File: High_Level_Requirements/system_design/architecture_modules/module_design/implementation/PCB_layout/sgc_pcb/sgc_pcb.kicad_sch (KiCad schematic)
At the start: 44 parts, among them J1 BAT_JST, Q1 PMOS_RFID, Q2 PMOS_UWB, SW1 Langir_16mm_Piezo, U1 LDC1612DNTR, U10 74AHCT1G125, U11 IP6833, U4 MT3608, U5 BHI260AP, U6 BMP390, U7 MX25R1635F, U8 IS31FL3194, U9 BQ25120A

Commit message: hw(v4.2): MX25R6435F 8MB flash + USB-C charging (drop Qi, beeper DNP)
- Flash U7: MX25R1635F (2MB) -> MX25R6435F (8MB), pin-compatible SOIC-8
  208-mil + JEDEC SPI/SFDP. Firmware auto-detects size (other session).
- Qi receiver (IP6833 + coil + passives) -> DNP; replaced by USB-C charging
  (GCT USB4085-GF-A, CC 5.1k sink pull-downs, ESD TVS, IP67 tethered cap).
- Beeper BZ1 -> DNP (footprint retained).
- Battery JST 3-pin flagged provisional.
- Discrepancy fixes: Y1 crystal + U6 BMP390 added to ref, stale "Reed
  Switch" label -> Langir piezo, rev v1.0 -> v4.2.
- New doc: sgc_usb_c_charging_spec.md.
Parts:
- removed U7: MX25R1635F, Package_SO:SOIC-8_3.9x4.9mm_P1.27mm, symbol sgc_pcb_symbols:MX25R1635F
- added C_USB: 10uF, Capacitor_SMD:C_0805_2012Metric, symbol Device:C
- added J2: USB4085, Connector_USB:USB_C_Receptacle_USB2.0, symbol Connector:USB_C_Receptacle_USB2.0
- added R_CC1, R_CC2: 5.1k, Resistor_SMD:R_0402_1005Metric, symbol Device:R
- added U7: MX25R6435F, Package_SO:SOIC-8_5.23x5.23mm_P1.27mm, symbol sgc_pcb_symbols:MX25R6435F
- added Y1: 32.768kHz, Crystal:Crystal_SMD_3215-2Pin_3.2x1.5mm, symbol Device:Crystal
- BZ1, C_AC1, C_AC2, C_BOOT, C_RECT, C_VDD, L3, U11: now not fitted; now left out of the parts list
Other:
- note added: "Sheet 2 — Sensors: Langir Piezo Button (v1 arming) + LDC1612 (v2, DNP)"
- note added: "Sheet 3 — Peripherals: SK6812 ×5 + Level Shifter + Beeper (DNP)"
- note added: "Sheet 4 — Power: Boost MT3608 + Battery JST + USB-C Charging (Qi DNP)"
- note removed: "Sheet 2 — Sensors: Reed Switch (v1 arming) + LDC1612 (v2, DNP)"
- note removed: "Sheet 3 — Peripherals: SK6812 ×5 + Level Shifter + Beeper"
- note removed: "Sheet 4 — Power: Boost MT3608 + Qi IP6833 + Battery JST"
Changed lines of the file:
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@@
   (title_block
     (title "SGC — Ski Gate Chrono")
-    (date "2026-08-12")
-    (rev "v1.0")
+    (date "2026-08-13")
+    (rev "v4.2")
     (company "VYT Solutions")
     (comment 1 "Custom PCB — Nicla Sense ME Replica")
-    (comment 2 "22 × 55 mm, 4-layer FR4, 0.8 mm")
+    (comment 2 "22 × 55 mm, 4-layer FR4, 0.8 mm — 8 MB flash + USB-C charging")
   )
   (symbol (lib_id "sgc_pcb_symbols:ANNA-B112") (at 200 300 0) (unit 1)
@@
     (instances (project "sgc_pcb" (path "/a1b2c3d4-e5f6-4a7b-8c9d-0e1f2a3b4c5d" (reference "MD1") (unit 1))))
   )
+  (symbol (lib_id "Device:Crystal") (at 150 200 0) (unit 1)
+    (exclude_from_sim no) (in_bom yes) (on_board yes) (dnp no)
+    (property "Reference" "Y1" (at 150 160 0) (effects (font (size 1.27 1.27))))
+    (property "Value" "32.768kHz" (at 150 240 0) (effects (font (size 1.27 1.27))))
+    (property "Footprint" "Crystal:Crystal_SMD_3215-2Pin_3.2x1.5mm" (at 150 200 0) (effects (font (size 1.27 1.27)) hide))
+    (instances (project "sgc_pcb" (path "/a1b2c3d4-e5f6-4a7b-8c9d-0e1f2a3b4c5d" (reference "Y1") (unit 1))))
+  )
   (symbol (lib_id "sgc_pcb_symbols:BHI260AP") (at 600 300 0) (unit 1)
     (exclude_from_sim no) (in_bom yes) (on_board yes) (dnp no)
@@
     (instances (project "sgc_pcb" (path "/a1b2c3d4-e5f6-4a7b-8c9d-0e1f2a3b4c5d" (reference "U6") (unit 1))))
   )
-  (symbol (lib_id "sgc_pcb_symbols:MX25R1635F") (at 600 100 0) (unit 1)
+  (symbol (lib_id "sgc_pcb_symbols:MX25R6435F") (at 600 100 0) (unit 1)
     (exclude_from_sim no) (in_bom yes) (on_board yes) (dnp no)
     (property "Reference" "U7" (at 600 60 0) (effects (font (size 1.27 1.27))))
-    (property "Value" "MX25R1635F" (at 600 140 0) (effects (font (size 1.27 1.27))))
-    (property "Footprint" "Package_SO:SOIC-8_3.9x4.9mm_P1.27mm" (at 600 100 0) (effects (font (size 1.27 1.27)) hide))
+    (property "Value" "MX25R6435F" (at 600 140 0) (effects (font (size 1.27 1.27))))
+    (property "Footprint" "Package_SO:SOIC-8_5.23x5.23mm_P1.27mm" (at 600 100 0) (effects (font (size 1.27 1.27)) hide))
     (instances (project "sgc_pcb" (path "/a1b2c3d4-e5f6-4a7b-8c9d-0e1f2a3b4c5d" (reference "U7") (unit 1))))
   )
@@
   )
   (symbol (lib_id "sgc_pcb_symbols:Piezo_Transducer") (at 300 650 0) (unit 1)
-    (exclude_from_sim no) (in_bom yes) (on_board yes) (dnp no)
+    (exclude_from_sim no) (in_bom no) (on_board no) (dnp yes)
     (property "Reference" "BZ1" (at 300 610 0) (effects (font (size 1.27 1.27))))
     (property "Value" "Piezo_10x10" (at 300 690 0) (effects (font (size 1.27 1.27))))
@@
   )
   (symbol (lib_id "sgc_pcb_symbols:IP6833") (at 800 -300 0) (unit 1)
-    (exclude_from_sim no) (in_bom yes) (on_board yes) (dnp no)
+    (exclude_from_sim no) (in_bom no) (on_board no) (dnp yes)
     (property "Reference" "U11" (at 800 -340 0) (effects (font (size 1.27 1.27))))
     (property "Value" "IP6833" (at 800 -260 0) (effects (font (size 1.27 1.27))))
@@
   )
   (symbol (lib_id "sgc_pcb_symbols:Qi_Coil") (at 800 -500 0) (unit 1)
-    (exclude_from_sim no) (in_bom yes) (on_board yes) (dnp no)
+    (exclude_from_sim no) (in_bom no) (on_board no) (dnp yes)
     (property "Reference" "L3" (at 800 -540 0) (effects (font (size 1.27 1.27))))
     (property "Value" "24uH_A11" (at 800 -460 0) (effects (font (size 1.27 1.27))))
@@
     (instances (project "sgc_pcb" (path "/a1b2c3d4-e5f6-4a7b-8c9d-0e1f2a3b4c5d" (reference "J1") (unit 1))))
   )
+  (symbol (lib_id "Connector:USB_C_Receptacle_USB2.0") (at 800 -600 0) (unit 1)
+    (exclude_from_sim no) (in_bom yes) (on_board yes) (dnp no)
+    (property "Reference" "J2" (at 800 -640 0) (effects (font (size 1.27 1.27))))
+    (property "Value" "USB4085" (at 800 -560 0) (effects (font (size 1.27 1.27))))
+    (property "Footprint" "Connector_USB:USB_C_Receptacle_USB2.0" (at 800 -600 0) (effects (font (size 1.27 1.27)) hide))
+    (instances (project "sgc_pcb" (path "/a1b2c3d4-e5f6-4a7b-8c9d-0e1f2a3b4c5d" (reference "J2") (unit 1))))
+  )
   (symbol (lib_id "sgc_pcb_symbols:PMOS_Gate") (at 900 500 0) (unit 1)
     (exclude_from_sim no) (in_bom no) (on_board no) (dnp yes)
@@
   )
   (symbol (lib_id "Device:C") (at 850 -400 0) (unit 1)
-    (exclude_from_sim no) (in_bom yes) (on_board yes) (dnp no)
+    (exclude_from_sim no) (in_bom no) (on_board no) (dnp yes)
     (property "Reference" "C_AC1" (at 850 -440 0) (effects (font (size 1.27 1.27))))
     (property "Value" "22nF" (at 850 -360 0) (effects (font (size 1.27 1.27))))
@@
   )
   (symbol (lib_id "Device:C") (at 850 -450 0) (unit 1)
-    (exclude_from_sim no) (in_bom yes) (on_board yes) (dnp no)
+    (exclude_from_sim no) (in_bom no) (on_board no) (dnp yes)
     (property "Reference" "C_AC2" (at 850 -490 0) (effects (font (size 1.27 1.27))))
     (property "Value" "22nF" (at 850 -410 0) (effects (font (size 1.27 1.27))))
@@
   )
   (symbol (lib_id "Device:C") (at 900 -300 0) (unit 1)
-    (exclude_from_sim no) (in_bom yes) (on_board yes) (dnp no)
+    (exclude_from_sim no) (in_bom no) (on_board no) (dnp yes)
     (property "Reference" "C_RECT" (at 900 -340 0) (effects (font (size 1.27 1.27))))
     (property "Value" "22uF" (at 900 -260 0) (effects (font (size 1.27 1.27))))
@@
   )
   (symbol (lib_id "Device:C") (at 900 -350 0) (unit 1)
-    (exclude_from_sim no) (in_bom yes) (on_board yes) (dnp no)
+    (exclude_from_sim no) (in_bom no) (on_board no) (dnp yes)
     (property "Reference" "C_BOOT" (at 900 -390 0) (effects (font (size 1.27 1.27))))
     (property "Value" "100n" (at 900 -310 0) (effects (font (size 1.27 1.27))))
@@
   )
   (symbol (lib_id "Device:C") (at 900 -400 0) (unit 1)
-    (exclude_from_sim no) (in_bom yes) (on_board yes) (dnp no)
+    (exclude_from_sim no) (in_bom no) (on_board no) (dnp yes)
     (property "Reference" "C_VDD" (at 900 -440 0) (effects (font (size 1.27 1.27))))
     (property "Value" "1uF" (at 900 -360 0) (effects (font (size 1.27 1.27))))
@@
     (instances (project "sgc_pcb" (path "/a1b2c3d4-e5f6-4a7b-8c9d-0e1f2a3b4c5d" (reference "L_Boost") (unit 1))))
   )
+  (symbol (lib_id "Device:R") (at 900 -600 0) (unit 1)
+    (exclude_from_sim no) (in_bom yes) (on_board yes) (dnp no)
+    (property "Reference" "R_CC1" (at 900 -640 0) (effects (font (size 1.27 1.27))))
+    (property "Value" "5.1k" (at 900 -560 0) (effects (font (size 1.27 1.27))))
+    (property "Footprint" "Resistor_SMD:R_0402_1005Metric" (at 900 -600 0) (effects (font (size 1.27 1.27)) hide))
+    (instances (project "sgc_pcb" (path "/a1b2c3d4-e5f6-4a7b-8c9d-0e1f2a3b4c5d" (reference "R_CC1") (unit 1))))
+  )
+  (symbol (lib_id "Device:R") (at 900 -650 0) (unit 1)
+    (exclude_from_sim no) (in_bom yes) (on_board yes) (dnp no)
+    (property "Reference" "R_CC2" (at 900 -690 0) (effects (font (size 1.27 1.27))))
+    (property "Value" "5.1k" (at 900 -610 0) (effects (font (size 1.27 1.27))))
+    (property "Footprint" "Resistor_SMD:R_0402_1005Metric" (at 900 -650 0) (effects (font (size 1.27 1.27)) hide))
+    (instances (project "sgc_pcb" (path "/a1b2c3d4-e5f6-4a7b-8c9d-0e1f2a3b4c5d" (reference "R_CC2") (unit 1))))
+  )
+  (symbol (lib_id "Device:C") (at 900 -700 0) (unit 1)
+    (exclude_from_sim no) (in_bom yes) (on_board yes) (dnp no)
+    (property "Reference" "C_USB" (at 900 -740 0) (effects (font (size 1.27 1.27))))
+    (property "Value" "10uF" (at 900 -660 0) (effects (font (size 1.27 1.27))))
+    (property "Footprint" "Capacitor_SMD:C_0805_2012Metric" (at 900 -700 0) (effects (font (size 1.27 1.27)) hide))
+    (instances (project "sgc_pcb" (path "/a1b2c3d4-e5f6-4a7b-8c9d-0e1f2a3b4c5d" (reference "C_USB") (unit 1))))
+  )
   (symbol (lib_id "power:VCC_3V3") (at 700 -600 0) (unit 1)
     (exclude_from_sim no) (in_bom yes) (on_board yes) (dnp no)
@@
     (instances (project "sgc_pcb" (path "/a1b2c3d4-e5f6-4a7b-8c9d-0e1f2a3b4c5d" (reference "#PWR") (unit 1))))
   )
-  (symbol (lib_id "power:V_QI_5V") (at 1100 -600 0) (unit 1)
+  (symbol (lib_id "power:VBUS") (at 1100 -600 0) (unit 1)
     (exclude_from_sim no) (in_bom yes) (on_board yes) (dnp no)
     (property "Reference" "#PWR" (at 1100 -600 0) (effects (font (size 1.27 1.27)) hide))
-    (property "Value" "V_QI_5V" (at 1100 -570 0) (effects (font (size 1.27 1.27))))
+    (property "Value" "VBUS" (at 1100 -570 0) (effects (font (size 1.27 1.27))))
     (instances (project "sgc_pcb" (path "/a1b2c3d4-e5f6-4a7b-8c9d-0e1f2a3b4c5d" (reference "#PWR") (unit 1))))
   )
@@
     (property "Intersheetrefs" "${INTERSHEET_REFS}" (at 450 600 0) (effects (font (size 1.27 1.27)) hide))
   )
-  (global_label "V_QI_5V" (shape bidirectional) (at 550 600 0) (fields_autoplaced yes)
+  (global_label "VBUS" (shape bidirectional) (at 550 600 0) (fields_autoplaced yes)
     (effects (font (size 1.27 1.27)) (justify left))
     (property "Intersheetrefs" "${INTERSHEET_REFS}" (at 550 600 0) (effects (font (size 1.27 1.27)) hide))
@@
   (text "SGC — Custom PCB: Nicla Sense ME Replica (v1 pole-mount)" (at 200 1200 0) (effects (font (size 2.0 2.0) bold)))
   (text "Sheet 1 — MCU Core: ANNA-B112 + BHI260AP + BMP390 + Flash + RGB + Charger" (at 200 400 0) (effects (font (size 2.0 2.0) bold)))
-  (text "Sheet 2 — Sensors: Reed Switch (v1 arming) + LDC1612 (v2, DNP)" (at 100 -200 0) (effects (font (size 2.0 2.0) bold)))
-  (text "Sheet 3 — Peripherals: SK6812 ×5 + Level Shifter + Beeper" (at 100 750 0) (effects (font (size 2.0 2.0) bold)))
-  (text "Sheet 4 — Power: Boost MT3608 + Qi IP6833 + Battery JST" (at 600 -150 0) (effects (font (size 2.0 2.0) bold)))
+  (text "Sheet 2 — Sensors: Langir Piezo Button (v1 arming) + LDC1612 (v2, DNP)" (at 100 -200 0) (effects (font (size 2.0 2.0) bold)))
+  (text "Sheet 3 — Peripherals: SK6812 ×5 + Level Shifter + Beeper (DNP)" (at 100 750 0) (effects (font (size 2.0 2.0) bold)))
+  (text "Sheet 4 — Power: Boost MT3608 + Battery JST + USB-C Charging (Qi DNP)" (at 600 -150 0) (effects (font (size 2.0 2.0) bold)))
   (text "Sheet 5 — v2 Peripherals (UNPOPULATED): RFID + UWB power gates" (at 900 700 0) (effects (font (size 2.0 2.0) bold)))
 )

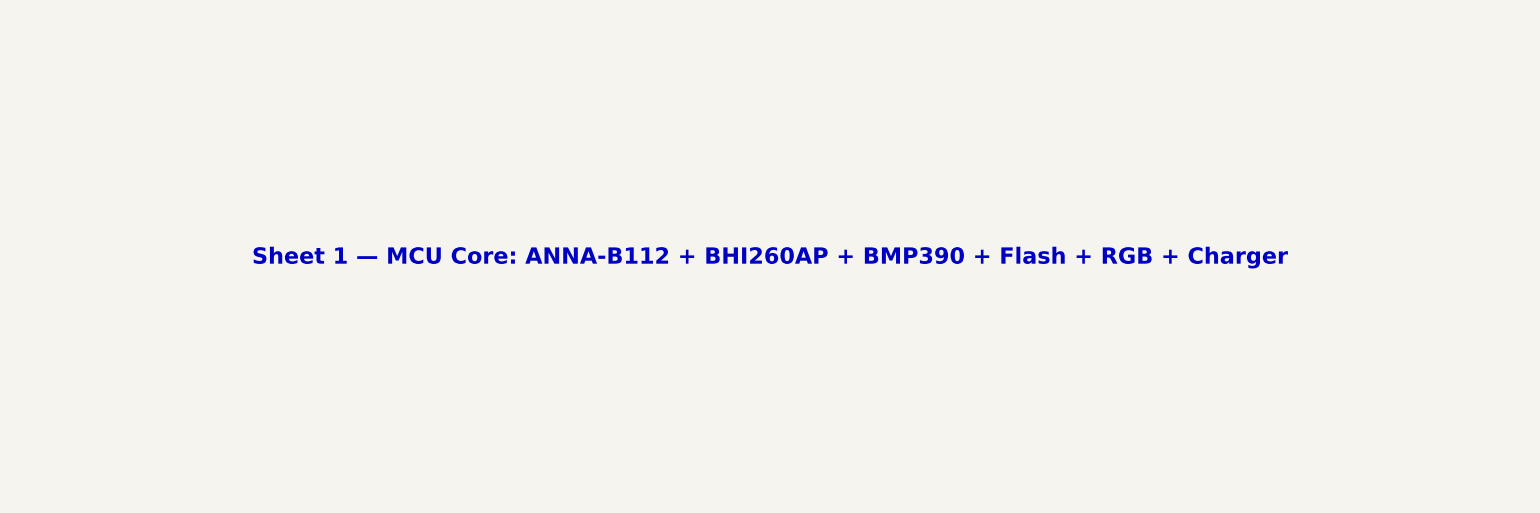
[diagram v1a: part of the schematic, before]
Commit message: hw: ANNA-B412 (nRF52833) as production MD1 — docs + schematic
Park production-module swap on branch until custom board exists.
Master stays Nicla/nRF52832 day-to-day. See anna_b412_migration.md.
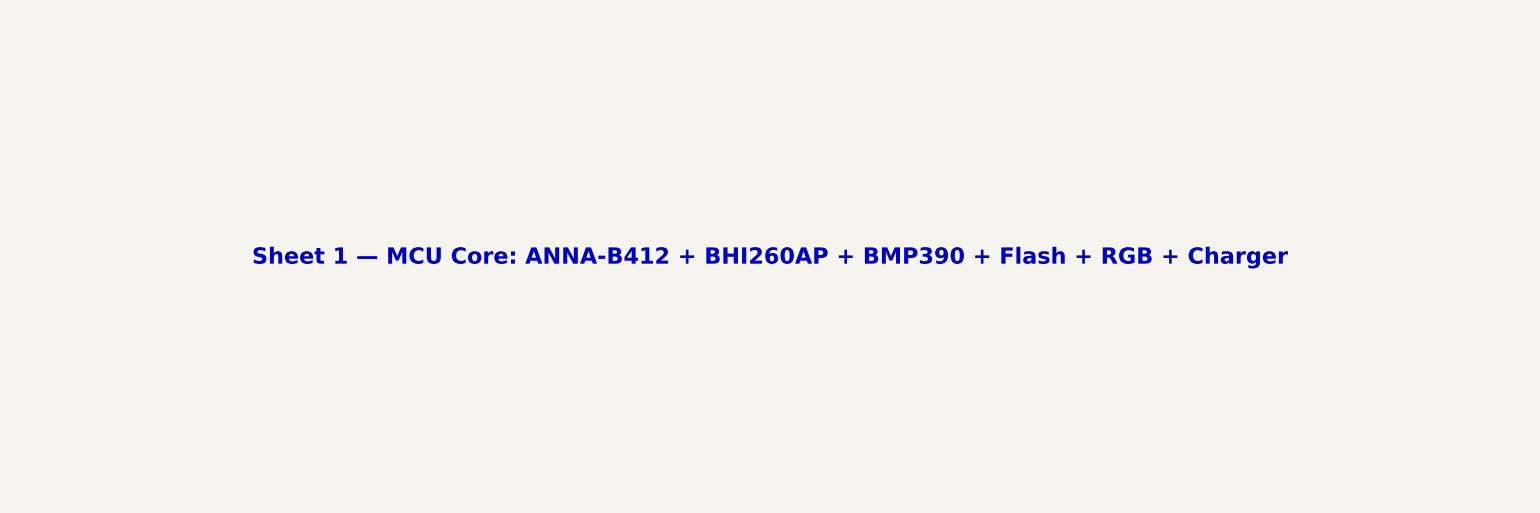
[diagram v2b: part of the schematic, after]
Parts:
- removed MD1: ANNA-B112, SGC:ANNA-B112, symbol sgc_pcb_symbols:ANNA-B112
- added MD1: ANNA-B412, SGC:ANNA-B412, symbol sgc_pcb_symbols:ANNA-B412
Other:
- note added: "Sheet 1 — MCU Core: ANNA-B412 + BHI260AP + BMP390 + Flash + RGB + Charger"
- note removed: "Sheet 1 — MCU Core: ANNA-B112 + BHI260AP + BMP390 + Flash + RGB + Charger"
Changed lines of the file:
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@@
   (title_block
     (title "SGC — Ski Gate Chrono")
-    (date "2026-08-13")
-    (rev "v4.2")
+    (date "2026-08-14")
+    (rev "v4.3")
     (company "VYT Solutions")
     (comment 1 "Custom PCB — Nicla Sense ME Replica")
     (comment 2 "22 × 55 mm, 4-layer FR4, 0.8 mm — 8 MB flash + USB-C charging")
   )
-  (symbol (lib_id "sgc_pcb_symbols:ANNA-B112") (at 200 300 0) (unit 1)
+  (symbol (lib_id "sgc_pcb_symbols:ANNA-B412") (at 200 300 0) (unit 1)
     (exclude_from_sim no) (in_bom yes) (on_board yes) (dnp no)
     (property "Reference" "MD1" (at 200 260 0) (effects (font (size 1.27 1.27))))
-    (property "Value" "ANNA-B112" (at 200 340 0) (effects (font (size 1.27 1.27))))
-    (property "Footprint" "SGC:ANNA-B112" (at 200 300 0) (effects (font (size 1.27 1.27)) hide))
+    (property "Value" "ANNA-B412" (at 200 340 0) (effects (font (size 1.27 1.27))))
+    (property "Footprint" "SGC:ANNA-B412" (at 200 300 0) (effects (font (size 1.27 1.27)) hide))
     (instances (project "sgc_pcb" (path "/a1b2c3d4-e5f6-4a7b-8c9d-0e1f2a3b4c5d" (reference "MD1") (unit 1))))
   )
@@
   )
   (text "SGC — Custom PCB: Nicla Sense ME Replica (v1 pole-mount)" (at 200 1200 0) (effects (font (size 2.0 2.0) bold)))
-  (text "Sheet 1 — MCU Core: ANNA-B112 + BHI260AP + BMP390 + Flash + RGB + Charger" (at 200 400 0) (effects (font (size 2.0 2.0) bold)))
+  (text "Sheet 1 — MCU Core: ANNA-B412 + BHI260AP + BMP390 + Flash + RGB + Charger" (at 200 400 0) (effects (font (size 2.0 2.0) bold)))
   (text "Sheet 2 — Sensors: Langir Piezo Button (v1 arming) + LDC1612 (v2, DNP)" (at 100 -200 0) (effects (font (size 2.0 2.0) bold)))
   (text "Sheet 3 — Peripherals: SK6812 ×5 + Level Shifter + Beeper (DNP)" (at 100 750 0) (effects (font (size 2.0 2.0) bold)))

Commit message: hw(anna-b412): DNP RV-3028-C7 external RTC footprint
Optional I2C RTC @ 0x52 on Wire (P0.22/23) with coin VBAT path.
Phone ABC0 remains primary time. Correct B412 GPIO budget note.
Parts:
- added BT1: CR1220_Holder, SGC:Coin_Cell_Holder_CR1220, symbol sgc_pcb_symbols:Coin_Cell_Holder
- added C_RTC1, C_RTC2: 100n, Capacitor_SMD:C_0603_1608Metric, symbol Device:C
- added R_RTC0: 0R, Resistor_SMD:R_0603_1608Metric, symbol Device:R
- added U12: RV-3028-C7, SGC:RV3028-C7_DFN-8, symbol sgc_pcb_symbols:RV3028-C7
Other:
- note added: "Sheet 6 — External RTC (DNP): RV-3028-C7 I2C @ 0x52 on Wire (P0.22/P0.23)"
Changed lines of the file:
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@@
     (instances (project "sgc_pcb" (path "/a1b2c3d4-e5f6-4a7b-8c9d-0e1f2a3b4c5d" (reference "Q2") (unit 1))))
+  )
+  (symbol (lib_id "sgc_pcb_symbols:RV3028-C7") (at 400 800 0) (unit 1)
+    (exclude_from_sim no) (in_bom no) (on_board no) (dnp yes)
+    (property "Reference" "U12" (at 400 760 0) (effects (font (size 1.27 1.27))))
+    (property "Value" "RV-3028-C7" (at 400 840 0) (effects (font (size 1.27 1.27))))
+    (property "Footprint" "SGC:RV3028-C7_DFN-8" (at 400 800 0) (effects (font (size 1.27 1.27)) hide))
+    (instances (project "sgc_pcb" (path "/a1b2c3d4-e5f6-4a7b-8c9d-0e1f2a3b4c5d" (reference "U12") (unit 1))))
+  )
+  (symbol (lib_id "sgc_pcb_symbols:Coin_Cell_Holder") (at 200 800 0) (unit 1)
+    (exclude_from_sim no) (in_bom no) (on_board no) (dnp yes)
+    (property "Reference" "BT1" (at 200 760 0) (effects (font (size 1.27 1.27))))
+    (property "Value" "CR1220_Holder" (at 200 840 0) (effects (font (size 1.27 1.27))))
+    (property "Footprint" "SGC:Coin_Cell_Holder_CR1220" (at 200 800 0) (effects (font (size 1.27 1.27)) hide))
+    (instances (project "sgc_pcb" (path "/a1b2c3d4-e5f6-4a7b-8c9d-0e1f2a3b4c5d" (reference "BT1") (unit 1))))
   )
   (symbol (lib_id "Device:C") (at 250 100 0) (unit 1)
@@
     (instances (project "sgc_pcb" (path "/a1b2c3d4-e5f6-4a7b-8c9d-0e1f2a3b4c5d" (reference "C_USB") (unit 1))))
   )
+  (symbol (lib_id "Device:C") (at 400 700 0) (unit 1)
+    (exclude_from_sim no) (in_bom no) (on_board no) (dnp yes)
+    (property "Reference" "C_RTC1" (at 400 660 0) (effects (font (size 1.27 1.27))))
+    (property "Value" "100n" (at 400 740 0) (effects (font (size 1.27 1.27))))
+    (property "Footprint" "Capacitor_SMD:C_0603_1608Metric" (at 400 700 0) (effects (font (size 1.27 1.27)) hide))
+    (instances (project "sgc_pcb" (path "/a1b2c3d4-e5f6-4a7b-8c9d-0e1f2a3b4c5d" (reference "C_RTC1") (unit 1))))
+  )
+  (symbol (lib_id "Device:C") (at 400 650 0) (unit 1)
+    (exclude_from_sim no) (in_bom no) (on_board no) (dnp yes)
+    (property "Reference" "C_RTC2" (at 400 610 0) (effects (font (size 1.27 1.27))))
+    (property "Value" "100n" (at 400 690 0) (effects (font (size 1.27 1.27))))
+    (property "Footprint" "Capacitor_SMD:C_0603_1608Metric" (at 400 650 0) (effects (font (size 1.27 1.27)) hide))
+    (instances (project "sgc_pcb" (path "/a1b2c3d4-e5f6-4a7b-8c9d-0e1f2a3b4c5d" (reference "C_RTC2") (unit 1))))
+  )
+  (symbol (lib_id "Device:R") (at 500 700 0) (unit 1)
+    (exclude_from_sim no) (in_bom no) (on_board no) (dnp yes)
+    (property "Reference" "R_RTC0" (at 500 660 0) (effects (font (size 1.27 1.27))))
+    (property "Value" "0R" (at 500 740 0) (effects (font (size 1.27 1.27))))
+    (property "Footprint" "Resistor_SMD:R_0603_1608Metric" (at 500 700 0) (effects (font (size 1.27 1.27)) hide))
+    (instances (project "sgc_pcb" (path "/a1b2c3d4-e5f6-4a7b-8c9d-0e1f2a3b4c5d" (reference "R_RTC0") (unit 1))))
+  )
   (symbol (lib_id "power:VCC_3V3") (at 700 -600 0) (unit 1)
     (exclude_from_sim no) (in_bom yes) (on_board yes) (dnp no)
@@
     (effects (font (size 1.27 1.27)) (justify left))
     (property "Intersheetrefs" "${INTERSHEET_REFS}" (at 450 1100 0) (effects (font (size 1.27 1.27)) hide))
+  )
+  (global_label "VBACKUP" (shape bidirectional) (at 650 900 0) (fields_autoplaced yes)
+    (effects (font (size 1.27 1.27)) (justify left))
+    (property "Intersheetrefs" "${INTERSHEET_REFS}" (at 650 900 0) (effects (font (size 1.27 1.27)) hide))
+  )
+  (global_label "RTC_INT" (shape bidirectional) (at 650 1000 0) (fields_autoplaced yes)
+    (effects (font (size 1.27 1.27)) (justify left))
+    (property "Intersheetrefs" "${INTERSHEET_REFS}" (at 650 1000 0) (effects (font (size 1.27 1.27)) hide))
   )
   (text "SGC — Custom PCB: Nicla Sense ME Replica (v1 pole-mount)" (at 200 1200 0) (effects (font (size 2.0 2.0) bold)))
@@
   (text "Sheet 4 — Power: Boost MT3608 + Battery JST + USB-C Charging (Qi DNP)" (at 600 -150 0) (effects (font (size 2.0 2.0) bold)))
   (text "Sheet 5 — v2 Peripherals (UNPOPULATED): RFID + UWB power gates" (at 900 700 0) (effects (font (size 2.0 2.0) bold)))
+  (text "Sheet 6 — External RTC (DNP): RV-3028-C7 I2C @ 0x52 on Wire (P0.22/P0.23)" (at 400 900 0) (effects (font (size 2.0 2.0) bold)))
 )
